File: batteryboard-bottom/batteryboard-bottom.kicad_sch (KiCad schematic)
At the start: 6 parts, among them J1 SLM-110-01-G-S, J2 FTS-105-01-L-DV-A

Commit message: Some changes
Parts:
- removed J1: SLM-110-01-G-S, batteryboard:SAMTEC_TMS-110-01-G-S, symbol Connector_Generic:Conn_01x10
- removed J2: FTS-105-01-L-DV-A, batteryboard:FTS-105-XX-YY-DV-A, symbol Connector_Generic:Conn_02x05_Odd_Even
- added J1: SFC-110-T2-F-D-A, mainboard:SAMTEC_SFC-110-T2-F-D-A-TR, symbol Connector_Generic:Conn_02x10_Odd_Even
- added J2: FTS-107-01-L-DV-A, batteryboard:SAMTEC-FTS-107-01-X-DV-A, symbol Connector_Generic:Conn_02x07_Odd_Even
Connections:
- net +3V3: now also J1.10 (Pin_10), J1.9 (Pin_9), J2.5 (Pin_5), J2.7 (Pin_7)
- net BATT_N_SW: now also J1.11 (Pin_11), J1.12 (Pin_12), J2.2 (Pin_2), J2.4 (Pin_4)
- net BATT_P: now also J1.17 (Pin_17), J1.18 (Pin_18), J2.10 (Pin_10), J2.12 (Pin_12)
- net BATT_P_SW: now also J1.13 (Pin_13), J1.14 (Pin_14), J2.6 (Pin_6), J2.8 (Pin_8)
- net COIL5_N: now also J1.20 (Pin_20), J2.14 (Pin_14)
- net COIL5_P: now also J1.2 (Pin_2), J2.13 (Pin_13)
- net GND: now also J1.16 (Pin_16), J1.3 (Pin_3), J1.4 (Pin_4), J2.1 (Pin_1), J2.3 (Pin_3)
- new net COIL6_N: J1.1 (Pin_1)
- new net COIL6_P: J1.19 (Pin_19)
- new net PAYLOAD_EN: J1.15 (Pin_15)
- new net SCL1: J1.6 (Pin_6), J2.9 (Pin_9)
- new net SDA1: J1.8 (Pin_8), J2.11 (Pin_11)
- new net UART_RX: J1.7 (Pin_7)
- new net UART_TX: J1.5 (Pin_5)

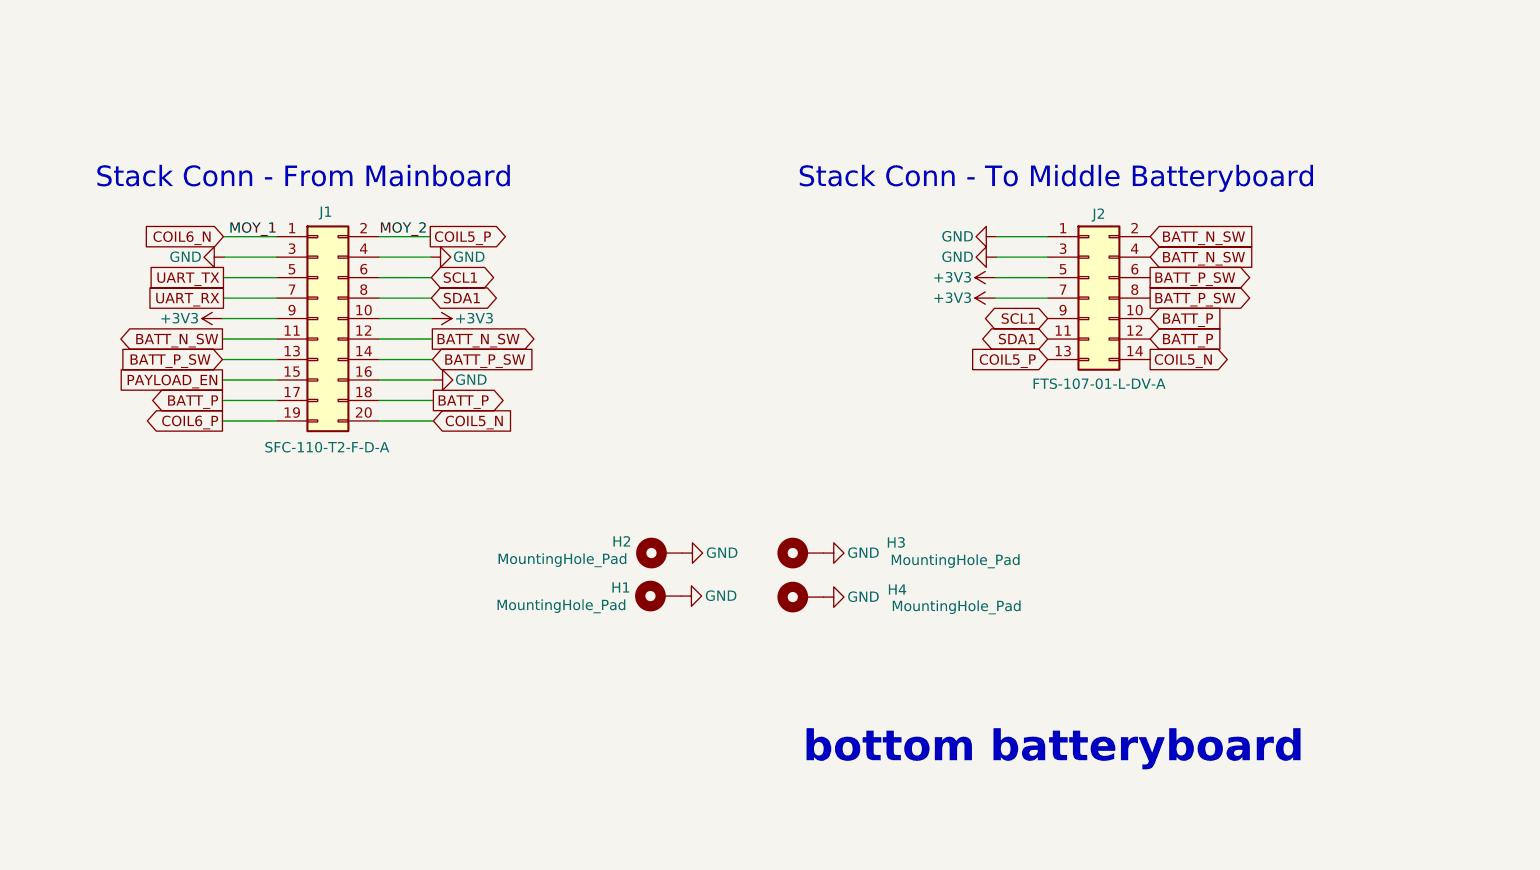
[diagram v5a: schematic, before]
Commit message: Updated batteryboards for Rev B3/01
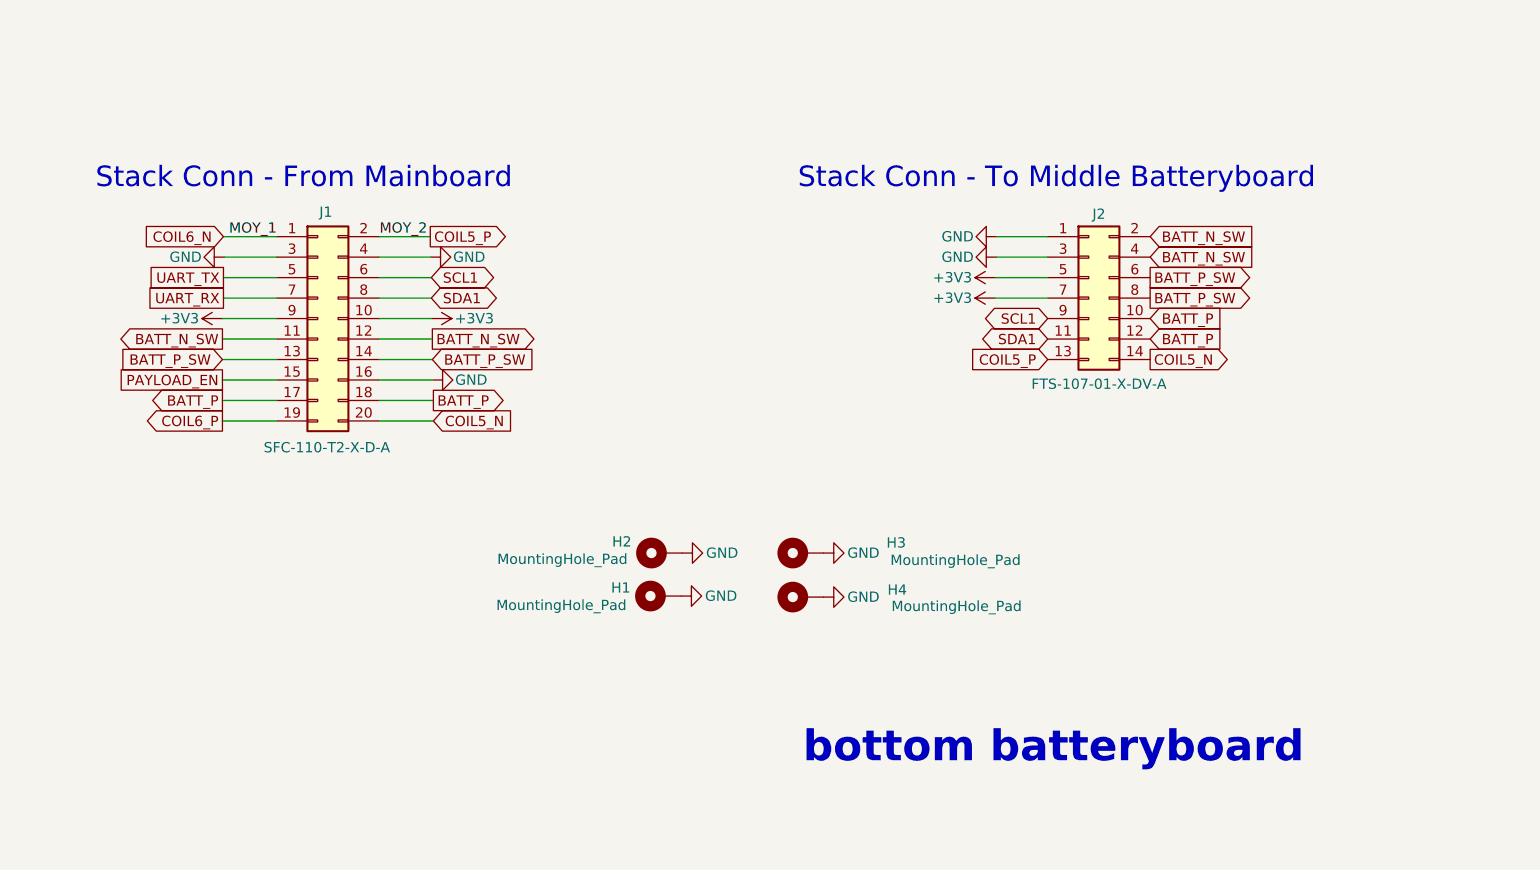
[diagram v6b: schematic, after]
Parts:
- J1: value SFC-110-T2-F-D-A -> SFC-110-T2-X-D-A; footprint mainboard:SAMTEC_SFC-110-T2-F-D-A-TR -> mainboard:SAMTEC_SFC-110-T2-X-D-A
- J2: value FTS-107-01-L-DV-A -> FTS-107-01-X-DV-A

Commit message: Added battery current sensing to bottom batteryboard
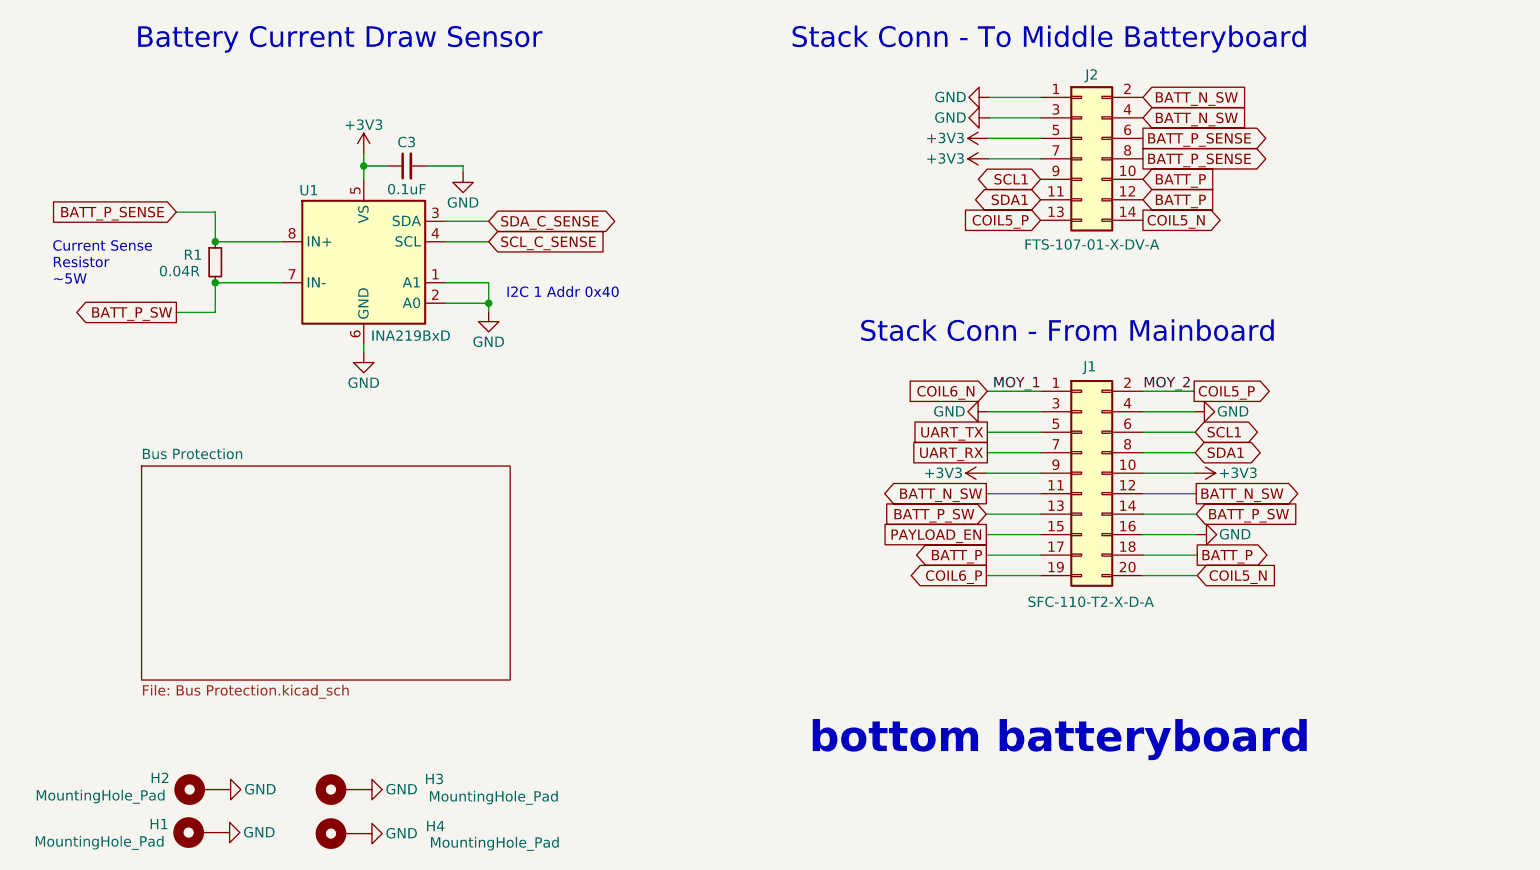
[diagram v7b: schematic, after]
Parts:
- added C3: 0.1uF, Capacitor_SMD:C_0603_1608Metric, symbol Device:C_Small
- added R1: 0.04R, Resistor_SMD:R_2512_6332Metric, symbol Device:R_Small
- added U1: INA219BxD, Package_SO:SOIC-8_3.9x4.9mm_P1.27mm, symbol Sensor_Energy:INA219BxD
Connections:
- net +3V3: now also C3.1, U1.5 (VS)
- net BATT_P_SW: now also R1.2, U1.7 (IN-); no longer J2.6 (Pin_6), J2.8 (Pin_8)
- net GND: now also C3.2, U1.1 (A1), U1.2 (A0), U1.6 (GND)
- new net BATT_P_SENSE: J2.6 (Pin_6), J2.8 (Pin_8), R1.1, U1.8 (IN+)
- new net SCL_C_SENSE: U1.4 (SCL)
- new net SDA_C_SENSE: U1.3 (SDA)
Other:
- added sheet Bus Protection (Bus Protection.kicad_sch)
- note added: "Battery Current Draw Sensor"
- note added: "Current Sense Resistor ~5W"
- note added: "I2C 1 Addr 0x40"
- moved on the sheet: H1, H2, H3, H4, J1, J2

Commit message: Rev B3/02 updates
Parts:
- R1: footprint Resistor_SMD:R_2512_6332Metric -> batteryboard:R_2512_CurrentSense
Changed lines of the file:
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@@
   (title_block
     (title "PyCubed Mini")
-    (date "2023-02-18")
-    (rev "B3/01")
+    (date "2023-04-12")
+    (rev "B3/02")
     (company "RExLab Carnegie Mellon University")
     (comment 1 "N. Khera")
@@
       (effects (font (size 1.27 1.27)) (justify left))
     )
-    (property "Footprint" "Resistor_SMD:R_2512_6332Metric" (at 40.386 52.578 0)
-      (effects (font (size 1.27 1.27)) hide)
-    )
+    (property "Footprint" "batteryboard:R_2512_CurrentSense" (at 40.386 52.578 0)
+      (effects (font (size 1.27 1.27)) hide)
+    )
